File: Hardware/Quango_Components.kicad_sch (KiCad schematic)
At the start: 97 parts, among them J1 Conn_01x12_Male, J2 Conn_01x12_Male, J3 Conn_01x12_Male, J4 Conn_01x12_Male, J5 SWD_Header, J6 Eurorack_10_pin_power, Q1 MMBT3904, U1 LM1117-3.3, U2 STM32G473V, U3 LM1117-5.0, U4 PS508, U5 MCP6002, U6 AS3364, U7 AS3364, U8 AD5676, U9 MCP48CMB21, Y1 8MHz 20pF

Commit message: Further Layout
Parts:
- added C51, C53: 100nF, Capacitor_SMD:C_0603_1608Metric, symbol Device:C_Small
- added C52, C54: 10uF, Capacitor_SMD:C_0805_2012Metric, symbol Device:C_Small
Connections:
- net +3.3V: now also C53.1, C54.1
- net +3.3VA: now also C51.1, C52.1
- net GND: now also C51.2, C52.2, C53.2, C54.2
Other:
- moved on the sheet: C47, C49

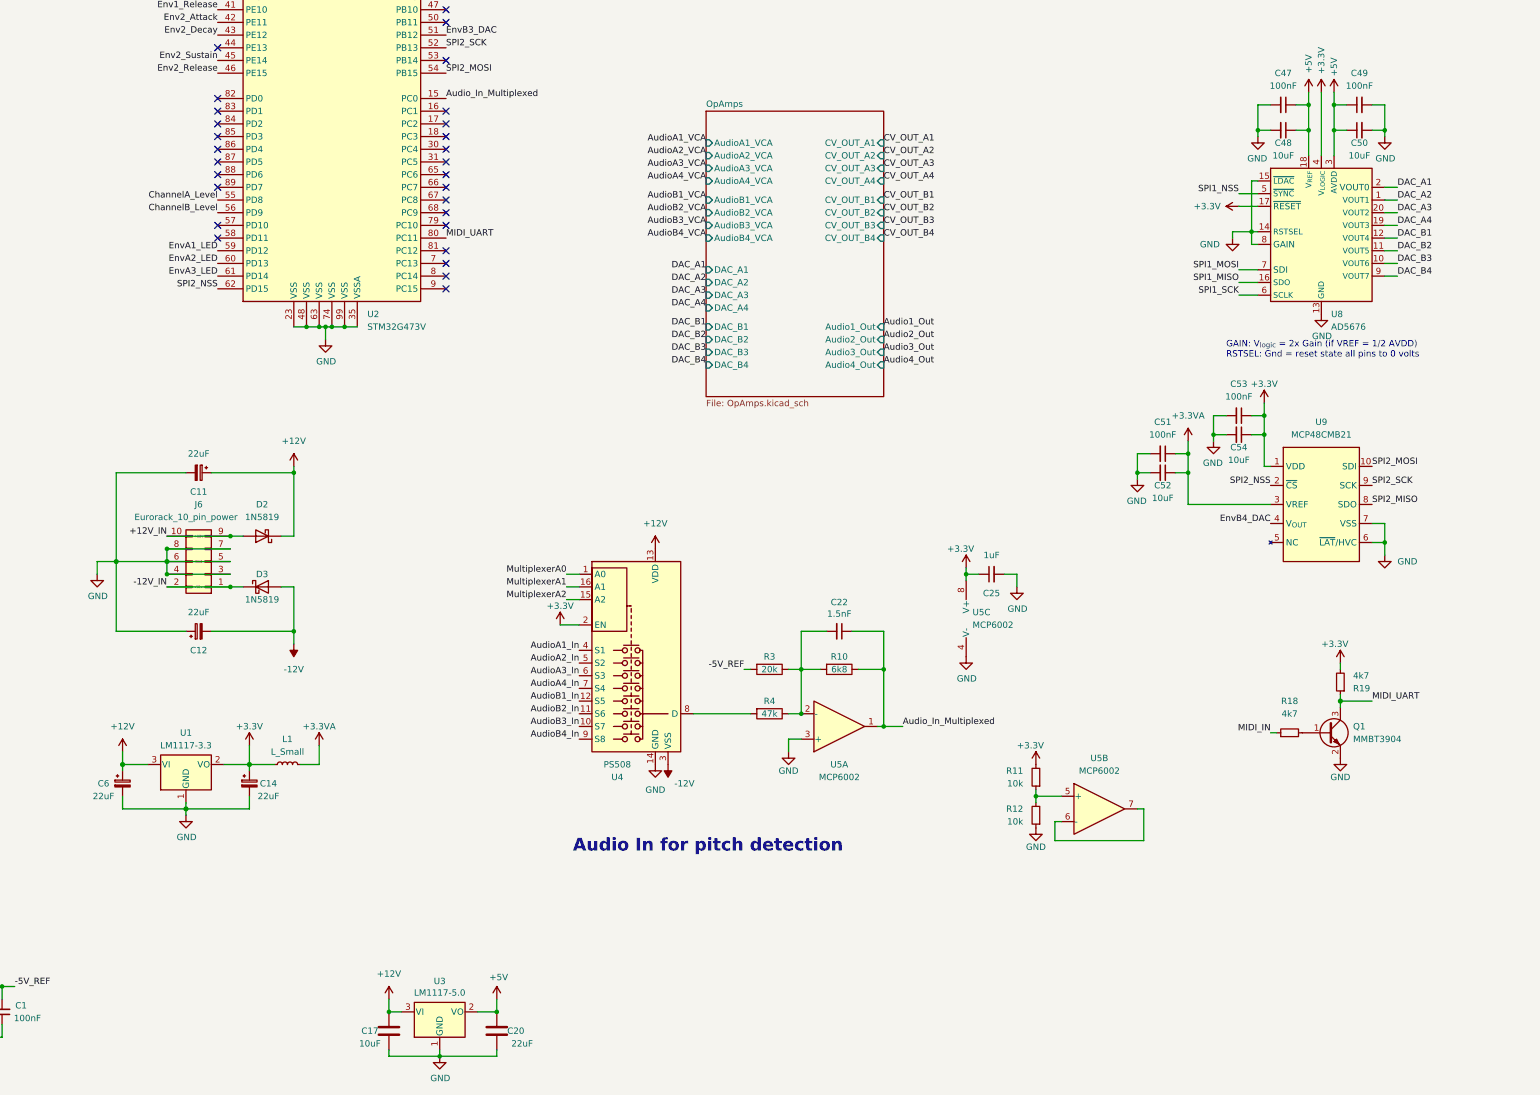
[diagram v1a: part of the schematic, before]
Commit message: Main components positioned
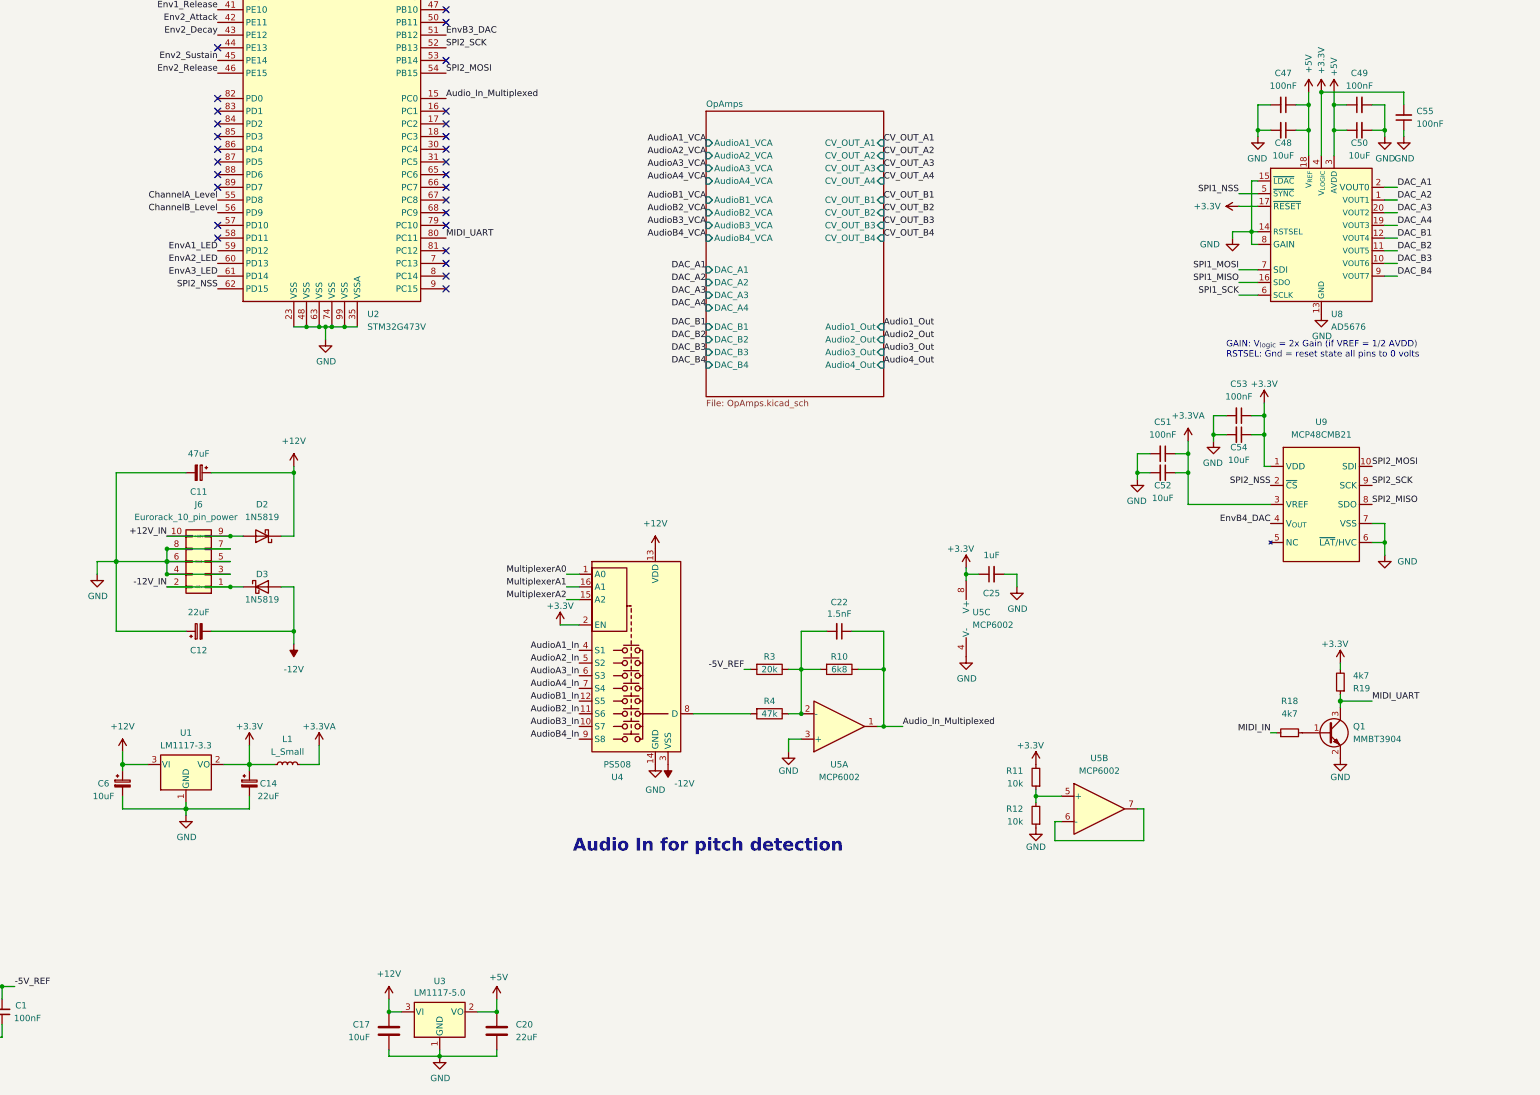
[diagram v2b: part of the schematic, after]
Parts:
- added C55: 100nF, Capacitor_SMD:C_0603_1608Metric, symbol Device:C_Small
- C11: value 22uF -> 47uF
- C17: footprint Capacitor_SMD:C_0805_2012Metric -> Capacitor_SMD:C_1206_3216Metric
- C6: value 22uF -> 10uF; footprint Capacitor_SMD:CP_Elec_4x5.8 -> Capacitor_SMD:C_1206_3216Metric
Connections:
- net +3.3V: now also C55.2
- net GND: now also C55.1
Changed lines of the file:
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@@
   (junction (at 193.04 81.28) (diameter 1.016) (color 0 0 0 0)
   )
+  (junction (at 274.32 128.27) (diameter 0) (color 0 0 0 0)
+  )
   (junction (at 73.66 35.56) (diameter 0) (color 0 0 0 0)
   )
@@
     (stroke (width 0) (type default) (color 0 0 0 0))
   )
+  (wire (pts (xy 290.83 137.16) (xy 290.83 135.89))
+    (stroke (width 0) (type default) (color 0 0 0 0))
+  )
   (wire (pts (xy 181.61 243.84) (xy 186.69 243.84))
     (stroke (width 0) (type default) (color 0 0 0 0))
@@
     (stroke (width 0) (type default) (color 0 0 0 0))
   )
+  (wire (pts (xy 290.83 128.27) (xy 290.83 130.81))
+    (stroke (width 0) (type default) (color 0 0 0 0))
+  )
   (wire (pts (xy 52.07 204.47) (xy 68.58 204.47))
     (stroke (width 0) (type solid) (color 0 0 0 0))
@@
     (stroke (width 0) (type solid) (color 0 0 0 0))
   )
+  (wire (pts (xy 274.32 128.27) (xy 290.83 128.27))
+    (stroke (width 0) (type default) (color 0 0 0 0))
+  )
   (wire (pts (xy 278.13 242.57) (xy 278.13 243.84))
     (stroke (width 0) (type default) (color 0 0 0 0))
@@
     (effects (font (size 1.27 1.27)) (justify left bottom))
   )
+  (symbol (lib_id "Device:C_Small") (at 290.83 133.35 180) (unit 1)
+    (in_bom yes) (on_board yes) (fields_autoplaced)
+    (property "Reference" "C55" (id 0) (at 293.37 132.0735 0)
+      (effects (font (size 1.27 1.27)) (justify right))
+    )
+    (property "Value" "100nF" (id 1) (at 293.37 134.6135 0)
+      (effects (font (size 1.27 1.27)) (justify right))
+    )
+    (property "Footprint" "Capacitor_SMD:C_0603_1608Metric" (id 2) (at 290.83 133.35 0)
+      (effects (font (size 1.27 1.27)) hide)
+    )
+    (property "Datasheet" "~" (id 3) (at 290.83 133.35 0)
+      (effects (font (size 1.27 1.27)) hide)
+    )
+    (pin "1")
+    (pin "2")
+  )
   (symbol (lib_id "power:+12V") (at 193.04 25.4 0) (unit 1)
     (in_bom yes) (on_board yes) (fields_autoplaced)
@@
     (pin "1")
   )
+  (symbol (lib_id "power:GND") (at 290.83 137.16 0) (unit 1)
+    (in_bom yes) (on_board yes)
+    (property "Reference" "#PWR0119" (id 0) (at 290.83 143.51 0)
+      (effects (font (size 1.27 1.27)) hide)
+    )
+    (property "Value" "GND" (id 1) (at 290.957 141.5542 0))
+    (property "Footprint" "" (id 2) (at 290.83 137.16 0)
+      (effects (font (size 1.27 1.27)) hide)
+    )
+    (property "Datasheet" "" (id 3) (at 290.83 137.16 0)
+      (effects (font (size 1.27 1.27)) hide)
+    )
+    (pin "1")
+  )
   (symbol (lib_id "power:GND") (at 199.39 34.29 0) (unit 1)
     (in_bom yes) (on_board yes)
@@
     (in_bom yes) (on_board yes)
     (property "Reference" "C11" (id 0) (at 49.53 208.28 90))
-    (property "Value" "22uF" (id 1) (at 49.53 200.66 90))
+    (property "Value" "47uF" (id 1) (at 49.53 200.66 90))
     (property "Footprint" "Capacitor_SMD:CP_Elec_4x5.8" (id 2) (at 49.53 204.47 0)
       (effects (font (size 1.27 1.27)) hide)
@@
   )
   (symbol (lib_id "Device:C") (at 109.22 316.23 0) (unit 1)
-    (in_bom yes) (on_board yes)
-    (property "Reference" "C20" (id 0) (at 113.03 316.23 0))
-    (property "Value" "22uF" (id 1) (at 114.3 318.77 0))
+    (in_bom yes) (on_board yes) (fields_autoplaced)
+    (property "Reference" "C20" (id 0) (at 113.03 314.9599 0)
+      (effects (font (size 1.27 1.27)) (justify left))
+    )
+    (property "Value" "22uF" (id 1) (at 113.03 317.4999 0)
+      (effects (font (size 1.27 1.27)) (justify left))
+    )
     (property "Footprint" "Capacitor_SMD:CP_Elec_4x5.8" (id 2) (at 110.1852 320.04 0)
       (effects (font (size 1.27 1.27)) hide)
@@
     (in_bom yes) (on_board yes)
     (property "Reference" "C6" (id 0) (at 30.48 266.7 0))
-    (property "Value" "22uF" (id 1) (at 30.48 269.24 0))
-    (property "Footprint" "Capacitor_SMD:CP_Elec_4x5.8" (id 2) (at 34.29 266.7 0)
+    (property "Value" "10uF" (id 1) (at 30.48 269.24 0))
+    (property "Footprint" "Capacitor_SMD:C_1206_3216Metric" (id 2) (at 34.29 266.7 0)
       (effects (font (size 1.27 1.27)) hide)
     )
@@
   )
   (symbol (lib_id "Device:C") (at 87.63 316.23 0) (unit 1)
-    (in_bom yes) (on_board yes)
-    (property "Reference" "C17" (id 0) (at 83.82 316.23 0))
-    (property "Value" "10uF" (id 1) (at 83.82 318.77 0))
-    (property "Footprint" "Capacitor_SMD:C_0805_2012Metric" (id 2) (at 88.5952 320.04 0)
+    (in_bom yes) (on_board yes) (fields_autoplaced)
+    (property "Reference" "C17" (id 0) (at 83.82 314.9599 0)
+      (effects (font (size 1.27 1.27)) (justify right))
+    )
+    (property "Value" "10uF" (id 1) (at 83.82 317.4999 0)
+      (effects (font (size 1.27 1.27)) (justify right))
+    )
+    (property "Footprint" "Capacitor_SMD:C_1206_3216Metric" (id 2) (at 88.5952 320.04 0)
       (effects (font (size 1.27 1.27)) hide)
     )
@@
       (reference "#PWR0118") (unit 1) (value "GND") (footprint "")
     )
+    (path "/300a041b-73b2-4711-a5e9-833c6d619710"
+      (reference "#PWR0119") (unit 1) (value "GND") (footprint "")
+    )
     (path "/6eb6111f-138a-445b-b2db-4b638f763c5a"
       (reference "C1") (unit 1) (value "100nF") (footprint "Capacitor_SMD:C_0603_1608Metric")
@@
     )
     (path "/dc781aca-880d-4b06-b79b-674f786382fe"
-      (reference "C6") (unit 1) (value "22uF") (footprint "Capacitor_SMD:CP_Elec_4x5.8")
+      (reference "C6") (unit 1) (value "10uF") (footprint "Capacitor_SMD:C_1206_3216Metric")
     )
     (path "/bbdd926f-4e22-46b1-8eef-14725340867b"
@@
     )
     (path "/3c78f1c2-2f26-409f-910c-ac67b9c082bb"
-      (reference "C11") (unit 1) (value "22uF") (footprint "Capacitor_SMD:CP_Elec_4x5.8")
+      (reference "C11") (unit 1) (value "47uF") (footprint "Capacitor_SMD:CP_Elec_4x5.8")
     )
     (path "/ffc62515-8361-4bbb-9353-71457f6d64ed"
@@
     )
     (path "/fc08ad2c-054a-45d5-8d7d-d4ee143f4c7f"
-      (reference "C17") (unit 1) (value "10uF") (footprint "Capacitor_SMD:C_0805_2012Metric")
+      (reference "C17") (unit 1) (value "10uF") (footprint "Capacitor_SMD:C_1206_3216Metric")
     )
     (path "/0684e8b7-49f8-4ac5-bfa6-a1558a0edcf6"
@@
       (reference "C54") (unit 1) (value "10uF") (footprint "Capacitor_SMD:C_0805_2012Metric")
     )
+    (path "/00ba52d9-d298-4d91-b62d-6f4e9f1cccb1"
+      (reference "C55") (unit 1) (value "100nF") (footprint "Capacitor_SMD:C_0603_1608Metric")
+    )
     (path "/1e372b72-4576-438a-8fd0-fffb7513b708"

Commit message: Added LED resistors
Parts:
- added R76, R77, R78, R79, R80, R81, R82, R83: 560, Resistor_SMD:R_0603_1608Metric, symbol Device:R
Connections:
- net CV_OUT_A1: now also J4.1 (Pin_1); no longer J3.1 (Pin_1)
- net CV_OUT_A2: now also J4.2 (Pin_2); no longer J3.2 (Pin_2)
- net CV_OUT_A3: now also J4.3 (Pin_3); no longer J3.3 (Pin_3)
- net CV_OUT_A4: now also J4.4 (Pin_4); no longer J3.4 (Pin_4)
- net CV_OUT_B1: now also J4.5 (Pin_5); no longer J3.5 (Pin_5)
- net CV_OUT_B2: now also J4.6 (Pin_6); no longer J3.6 (Pin_6)
- net CV_OUT_B3: now also J4.7 (Pin_7); no longer J3.7 (Pin_7)
- net CV_OUT_B4: now also J4.8 (Pin_8); no longer J3.8 (Pin_8)
- net Env1_Attack: now also J1.1 (Pin_1); no longer J4.1 (Pin_1)
- net Env1_Decay: now also J1.2 (Pin_2); no longer J4.2 (Pin_2)
- net Env1_Release: now also J1.4 (Pin_4); no longer J4.4 (Pin_4)
- net Env1_Sustain: now also J1.3 (Pin_3); no longer J4.3 (Pin_3)
- net Env2_Attack: now also J1.5 (Pin_5); no longer J4.5 (Pin_5)
- net Env2_Decay: now also J1.6 (Pin_6); no longer J4.6 (Pin_6)
- net Env2_Release: now also J1.8 (Pin_8); no longer J4.8 (Pin_8)
- net Env2_Sustain: now also J1.7 (Pin_7); no longer J4.7 (Pin_7)
- net EnvA1_LED: now also R76.2; no longer J1.1 (Pin_1)
- net EnvA2_LED: now also R77.2; no longer J1.2 (Pin_2)
- net EnvA3_LED: now also R78.2; no longer J1.3 (Pin_3)
- net EnvA4_LED: now also R79.2; no longer J1.4 (Pin_4)
- net EnvB1_LED: now also R80.2; no longer J1.5 (Pin_5)
- net EnvB2_LED: now also R81.2; no longer J1.6 (Pin_6)
- net EnvB3_LED: now also R82.2; no longer J1.7 (Pin_7)
- net EnvB4_LED: now also R83.2; no longer J1.8 (Pin_8)
- new net EnvA1_LED_Out: J3.1 (Pin_1), R76.1
- new net EnvA2_LED_Out: J3.2 (Pin_2), R77.1
- new net EnvA3_LED_Out: J3.3 (Pin_3), R78.1
- new net EnvA4_LED_Out: J3.4 (Pin_4), R79.1
- new net EnvB1_LED_Out: J3.5 (Pin_5), R80.1
- new net EnvB2_LED_Out: J3.6 (Pin_6), R81.1
- new net EnvB3_LED_Out: J3.7 (Pin_7), R82.1
- new net EnvB4_LED_Out: J3.8 (Pin_8), R83.1

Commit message: More Layout
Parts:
- added R84, R85: 560, Resistor_SMD:R_0603_1608Metric, symbol Device:R
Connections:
- net +3.3VA: now also J4.1 (Pin_1); no longer J4.9 (Pin_9)
- net CV_OUT_A1: now also J4.6 (Pin_6); no longer J4.1 (Pin_1)
- net CV_OUT_A2: now also J4.5 (Pin_5); no longer J4.2 (Pin_2)
- net CV_OUT_A3: now also J4.8 (Pin_8); no longer J4.3 (Pin_3)
- net CV_OUT_A4: now also J4.7 (Pin_7); no longer J4.4 (Pin_4)
- net CV_OUT_B1: now also J4.10 (Pin_10); no longer J4.5 (Pin_5)
- net CV_OUT_B2: now also J4.9 (Pin_9); no longer J4.6 (Pin_6)
- net CV_OUT_B3: now also J4.12 (Pin_12); no longer J4.7 (Pin_7)
- net CV_OUT_B4: now also J4.11 (Pin_11); no longer J4.8 (Pin_8)
- net Calib_Btn1: now also J4.2 (Pin_2); no longer J4.10 (Pin_10)
- net Calib_Btn2: now also J4.3 (Pin_3); no longer J4.11 (Pin_11)
- net GND: now also J4.4 (Pin_4), R84.2, R85.2; no longer J4.12 (Pin_12), U8.15 (~{LDAC}), U9.6 (~{LAT}/HVC)
- new net: R85.1, U9.6 (~{LAT}/HVC)
- new net: R84.1, U8.15 (~{LDAC})
